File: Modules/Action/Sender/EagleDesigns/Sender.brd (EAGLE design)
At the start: 100 x 80 mm, 10 parts, among them U2 ATMEGA328P_TQFP

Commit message: fixed eagle files for new modules
SIN/SOUT was not correctly connected in them.
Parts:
- R3: value 680 -> 100
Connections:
- removed net 1X3SIN: U2.23
- net 1X3SIN-SOUT: now also U2.23
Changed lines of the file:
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@@
 <attribute name="PROD_ID" value="IC-09069" x="10.1" y="12.54" size="1.778" layer="28" rot="MR0" display="off"/>
 </element>
-<element name="R3" library="adafruit" package="R0603" value="680" x="17.5" y="16" rot="MR0"/>
+<element name="R3" library="adafruit" package="R0603" value="100" x="17.5" y="16" rot="MR0"/>
 <element name="IRLED" library="SparkFun-LED" package="LED5MM" value="" x="20.8" y="10.8" rot="R270"/>
 </elements>
@@
 <wire x1="8.42" y1="4.02" x2="8.7" y2="4.3" width="0.3048" layer="1"/>
 <wire x1="8.7" y1="4.3" x2="15.8" y2="4.3" width="0.3048" layer="1"/>
+<contactref element="U2" pad="23"/>
+<wire x1="8.7" y1="4.3" x2="5.8074" y2="14.54" width="0" layer="19" extent="1-16"/>
 </signal>
 <signal name="RESET">
@@
 <wire x1="14.8" y1="20.15" x2="14.76" y2="20.39" width="0.3048" layer="16"/>
 </signal>
-<signal name="1X3SIN">
-<contactref element="U2" pad="23"/>
-</signal>
 <signal name="N$1">

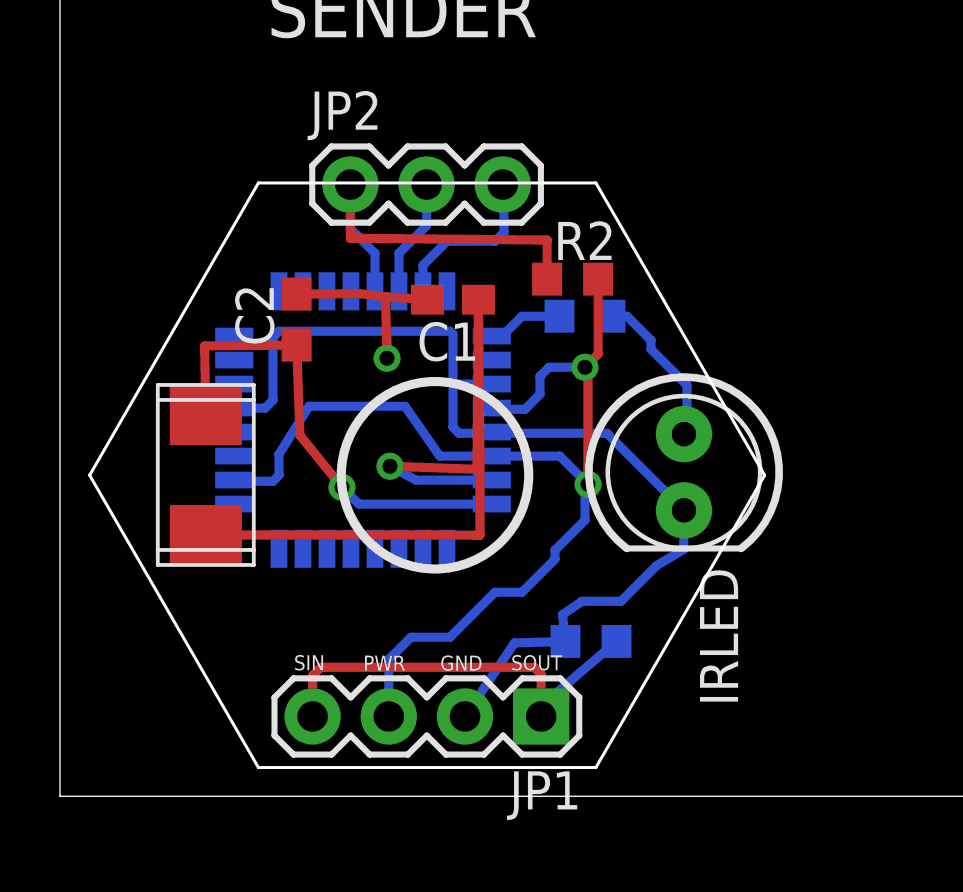
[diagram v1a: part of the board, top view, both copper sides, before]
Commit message: Sender: added final PCB #29
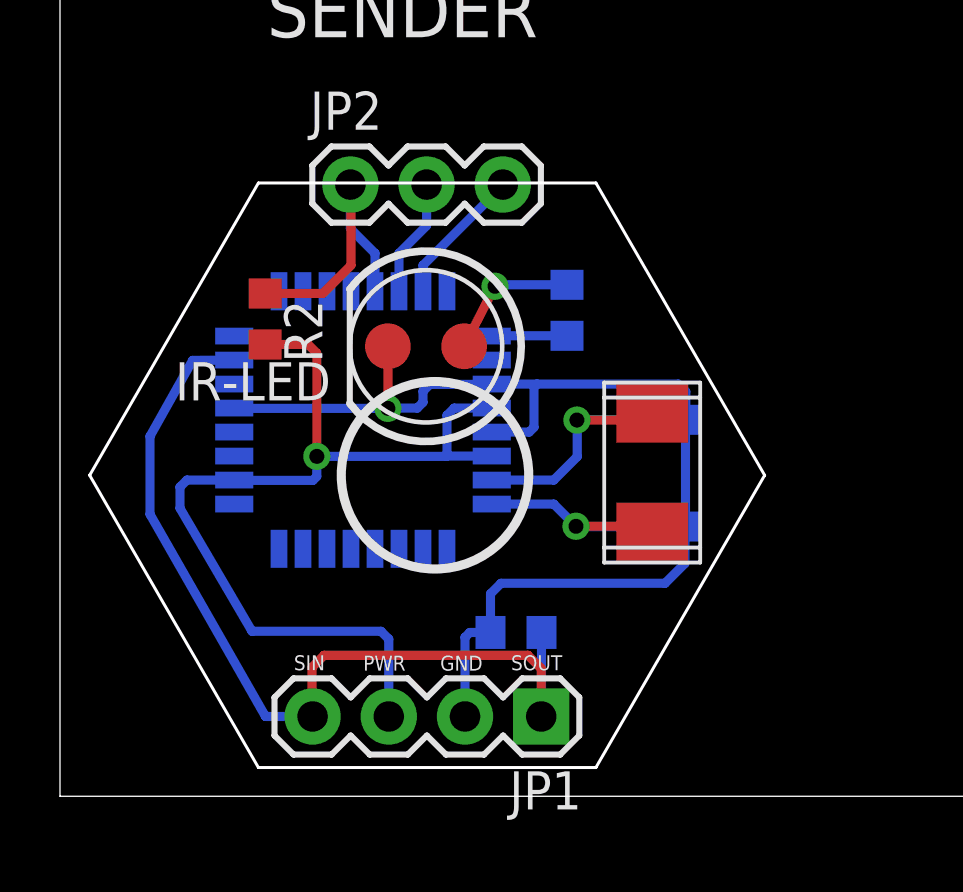
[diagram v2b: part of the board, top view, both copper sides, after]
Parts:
- removed IRLED: (no value), SparkFun-LED:LED5MM
- added IR-LED: LED-SMD, MakerWear:LED5MM-SMD
- moved U$2 14.9 mm to (19.7, 10.8), turned to 270 degrees
- moved C2 13.9 mm to (20.0, 8.99), flipped to the bottom, turned to 180 degrees
- moved R2 10.3 mm to (6.84, 15.9), turned to 270 degrees
- moved C1 7.98 mm to (20.0, 12.6), flipped to the bottom
- moved R1 2.52 mm to (15.2, 5.46)
- moved R3 0.63 mm to (16.9, 16.2), turned to 270 degrees
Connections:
- net GND: now also IR-LED.CATHODE; no longer IRLED.K
- net N$2: now also IR-LED.ANODE; no longer IRLED.A
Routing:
- net N$1: track 29.1 -> 8.93 mm
- net 1X3SIN-SOUT: track 14.4 -> 30.3 mm
- net N$3: track 15.8 -> 7.69 mm
- net VCC: track 37.6 -> 32.2 mm, vias 2 -> 1
- net GND: track 41.9 -> 38.2 mm
- net RESET: track 13.5 -> 9.84 mm
- net TX: track 5.62 -> 4.66 mm
- net N$2: track 5.35 -> 4.67 mm, vias 0 -> 1
